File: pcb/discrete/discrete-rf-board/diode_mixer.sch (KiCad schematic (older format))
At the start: 30 parts, among them J30 UFL, J31 UFL, J32 UFL, J33 UFL, T5 HHM17147A1, T6 HHM17147A1, U22 BAT15-099R

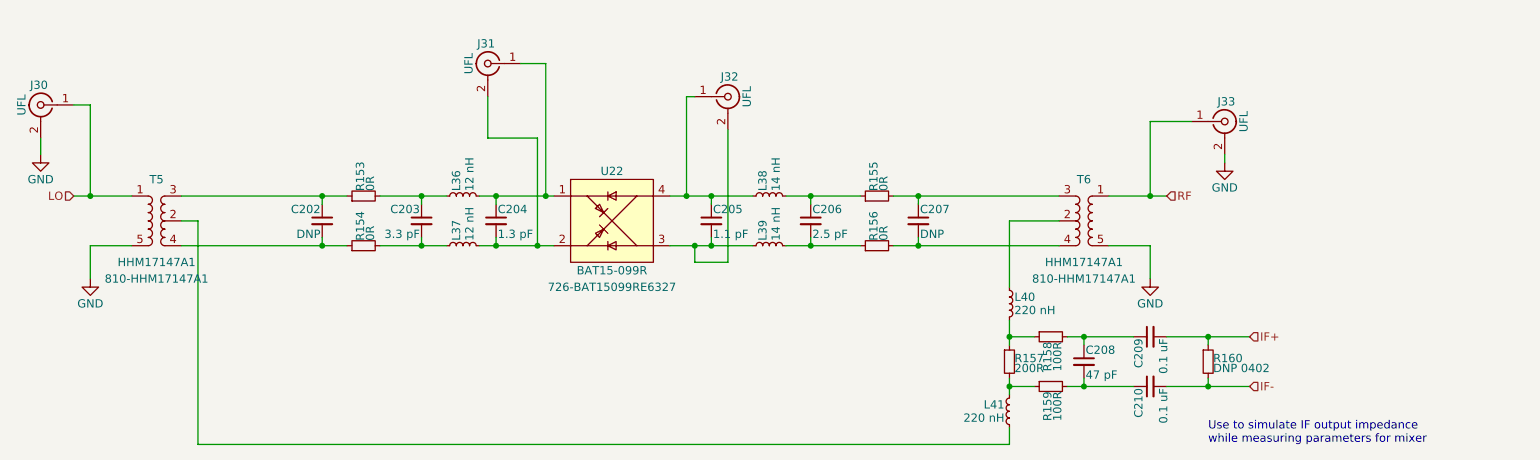
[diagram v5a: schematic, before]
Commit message: All component values set (TODO change transistor gain stages to match values from experimentation
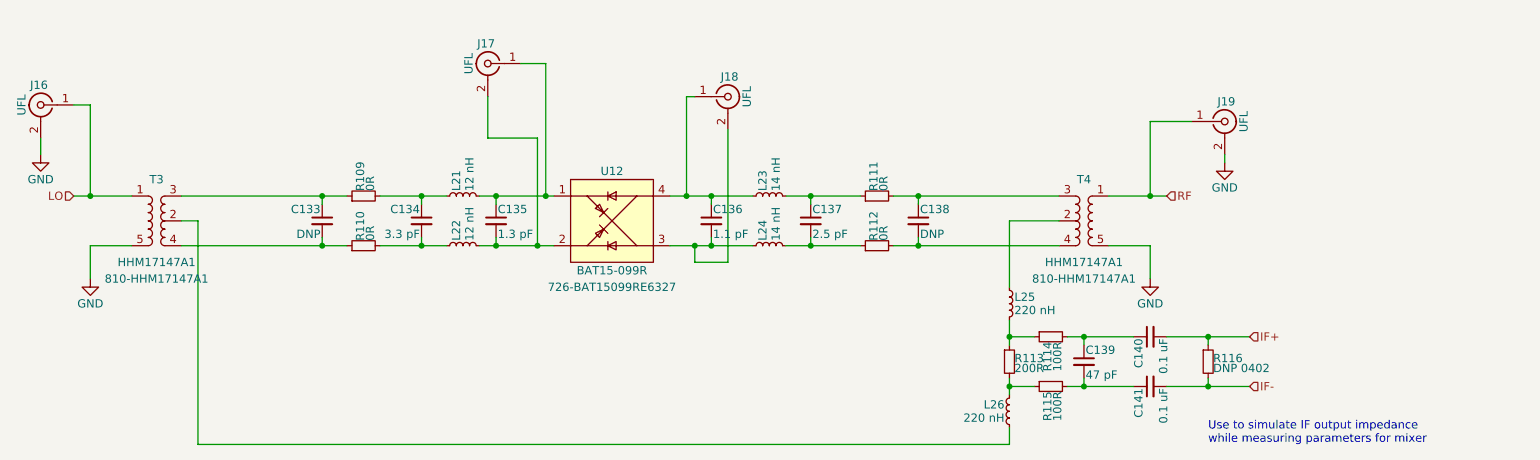
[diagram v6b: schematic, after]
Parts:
- T6: footprint (none) -> discrete_footprints:TDK_HHM17147A1
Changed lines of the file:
@@
 $Descr A4 11693 8268
 encoding utf-8
-Sheet 19 19
+Sheet 11 19
 Title ""
 Date ""
@@
 AR Path="/5CA6B0AA/5CC1CC09/5CC1E322" Ref="U22"  Part="1"
 AR Path="/5CA6B0AA/5CC4015A/5CC1E322" Ref="U12"  Part="1"
-F 0 "U22" H 5900 3900 50  0000 C CNN
+F 0 "U12" H 5900 3900 50  0000 C CNN
 F 1 "BAT15-099R" H 5900 3300 50  0000 C CNN
 F 2 "discrete_footprints:Infineon_SOT143" H 5900 3900 50  0001 C CNN
@@
 AR Path="/5CA6B0AA/5CC1CC09/5CC1F89D" Ref="C205"  Part="1"
 AR Path="/5CA6B0AA/5CC4015A/5CC1F89D" Ref="C136"  Part="1"
-F 0 "C205" H 6510 3670 50  0000 L CNN
+F 0 "C136" H 6510 3670 50  0000 L CNN
 F 1 "1.1 pF" H 6510 3520 50  0000 L CNN
 F 2 "" H 6500 3600 50  0001 C CNN
@@
 AR Path="/5CA6B0AA/5CC1CC09/5CC20238" Ref="C206"  Part="1"
 AR Path="/5CA6B0AA/5CC4015A/5CC20238" Ref="C137"  Part="1"
-F 0 "C206" H 7110 3670 50  0000 L CNN
+F 0 "C137" H 7110 3670 50  0000 L CNN
 F 1 "2.5 pF" H 7110 3520 50  0000 L CNN
 F 2 "" H 7100 3600 50  0001 C CNN
@@
 AR Path="/5CA6B0AA/5CC1CC09/5CC208EE" Ref="L39"  Part="1"
 AR Path="/5CA6B0AA/5CC4015A/5CC208EE" Ref="L24"  Part="1"
-F 0 "L39" H 6880 3790 50  0000 L CNN
+F 0 "L24" H 6880 3790 50  0000 L CNN
 F 1 "14 nH" H 6880 3710 50  0000 L CNN
 F 2 "" H 6850 3750 50  0001 C CNN
@@
 AR Path="/5CA6B0AA/5CC1CC09/5CC2101C" Ref="L38"  Part="1"
 AR Path="/5CA6B0AA/5CC4015A/5CC2101C" Ref="L23"  Part="1"
-F 0 "L38" H 6880 3490 50  0000 L CNN
+F 0 "L23" H 6880 3490 50  0000 L CNN
 F 1 "14 nH" H 6880 3410 50  0000 L CNN
 F 2 "" H 6850 3450 50  0001 C CNN
@@
 AR Path="/5CA6B0AA/5CC1CC09/5CC289D9" Ref="L40"  Part="1"
 AR Path="/5CA6B0AA/5CC4015A/5CC289D9" Ref="L25"  Part="1"
-F 0 "L40" H 8330 4140 50  0000 L CNN
+F 0 "L25" H 8330 4140 50  0000 L CNN
 F 1 "220 nH" H 8330 4060 50  0000 L CNN
 F 2 "" H 8300 4100 50  0001 C CNN
@@
 AR Path="/5CA6B0AA/5CC1CC09/5CC29B4E" Ref="R157"  Part="1"
 AR Path="/5CA6B0AA/5CC4015A/5CC29B4E" Ref="R113"  Part="1"
-F 0 "R157" H 8330 4470 50  0000 L CNN
+F 0 "R113" H 8330 4470 50  0000 L CNN
 F 1 "200R" H 8330 4410 50  0000 L CNN
 F 2 "" H 8300 4450 50  0001 C CNN
@@
 AR Path="/5CA6B0AA/5CC1CC09/5CC29F9D" Ref="R158"  Part="1"
 AR Path="/5CA6B0AA/5CC4015A/5CC29F9D" Ref="R114"  Part="1"
-F 0 "R158" H 8580 4320 50  0000 L CNN
+F 0 "R114" H 8580 4320 50  0000 L CNN
 F 1 "100R" H 8580 4260 50  0000 L CNN
 F 2 "" H 8550 4300 50  0001 C CNN
@@
 AR Path="/5CA6B0AA/5CC1CC09/5CC2B0AC" Ref="C208"  Part="1"
 AR Path="/5CA6B0AA/5CC4015A/5CC2B0AC" Ref="C139"  Part="1"
-F 0 "C208" H 8760 4520 50  0000 L CNN
+F 0 "C139" H 8760 4520 50  0000 L CNN
 F 1 "47 pF" H 8760 4370 50  0000 L CNN
 F 2 "" H 8750 4450 50  0001 C CNN
@@
 AR Path="/5CA6B0AA/5CC1CC09/5CC2FA5E" Ref="#PWR0257"  Part="1"
 AR Path="/5CA6B0AA/5CC4015A/5CC2FA5E" Ref="#PWR0169"  Part="1"
-F 0 "#PWR0257" H 2750 3700 50  0001 C CNN
+F 0 "#PWR0169" H 2750 3700 50  0001 C CNN
 F 1 "GND" H 2750 3800 50  0000 C CNN
 F 2 "" H 2750 3950 50  0001 C CNN
@@
 AR Path="/5CA6B0AA/5CC1CC09/5CC3011D" Ref="#PWR0258"  Part="1"
 AR Path="/5CA6B0AA/5CC4015A/5CC3011D" Ref="#PWR0170"  Part="1"
-F 0 "#PWR0258" H 9150 3700 50  0001 C CNN
+F 0 "#PWR0170" H 9150 3700 50  0001 C CNN
 F 1 "GND" H 9150 3800 50  0000 C CNN
 F 2 "" H 9150 3950 50  0001 C CNN
@@
 AR Path="/5CA6B0AA/5CC1CC09/5CC30B27" Ref="J30"  Part="1"
 AR Path="/5CA6B0AA/5CC4015A/5CC30B27" Ref="J16"  Part="1"
-F 0 "J30" H 2460 3020 50  0000 C CNN
+F 0 "J16" H 2460 3020 50  0000 C CNN
 F 1 "UFL" V 2565 2900 50  0000 C CNN
 F 2 "" H 2450 2900 50  0001 C CNN
@@
 AR Path="/5CA6B0AA/5CC1CC09/5CC31787" Ref="J33"  Part="1"
 AR Path="/5CA6B0AA/5CC4015A/5CC31787" Ref="J19"  Part="1"
-F 0 "J33" H 9610 3120 50  0000 C CNN
+F 0 "J19" H 9610 3120 50  0000 C CNN
 F 1 "UFL" V 9715 3000 50  0000 C CNN
 F 2 "" H 9600 3000 50  0001 C CNN
@@
 AR Path="/5CA6B0AA/5CC1CC09/5CC33186" Ref="#PWR0259"  Part="1"
 AR Path="/5CA6B0AA/5CC4015A/5CC33186" Ref="#PWR0171"  Part="1"
-F 0 "#PWR0259" H 9600 3000 50  0001 C CNN
+F 0 "#PWR0171" H 9600 3000 50  0001 C CNN
 F 1 "GND" H 9600 3100 50  0000 C CNN
 F 2 "" H 9600 3250 50  0001 C CNN
@@
 AR Path="/5CA6B0AA/5CC1CC09/5CC33A73" Ref="#PWR0256"  Part="1"
 AR Path="/5CA6B0AA/5CC4015A/5CC33A73" Ref="#PWR0168"  Part="1"
-F 0 "#PWR0256" H 2450 2950 50  0001 C CNN
+F 0 "#PWR0168" H 2450 2950 50  0001 C CNN
 F 1 "GND" H 2450 3050 50  0000 C CNN
 F 2 "" H 2450 3200 50  0001 C CNN
@@
 AR Path="/5CA6B0AA/5CC1CC09/5CC5AE0B" Ref="L41"  Part="1"
 AR Path="/5CA6B0AA/5CC4015A/5CC5AE0B" Ref="L26"  Part="1"
-F 0 "L41" H 8330 4790 50  0000 L CNN
+F 0 "L26" H 8330 4790 50  0000 L CNN
 F 1 "220 nH" H 8330 4710 50  0000 L CNN
 F 2 "" H 8300 4750 50  0001 C CNN
@@
 AR Path="/5CA6B0AA/5CC1CC09/5CC5DD55" Ref="R159"  Part="1"
 AR Path="/5CA6B0AA/5CC4015A/5CC5DD55" Ref="R115"  Part="1"
-F 0 "R159" H 8580 4620 50  0000 L CNN
+F 0 "R115" H 8580 4620 50  0000 L CNN
 F 1 "100R" H 8580 4560 50  0000 L CNN
 F 2 "" H 8550 4600 50  0001 C CNN
@@
 AR Path="/5CA6B0AA/5CC1CC09/5CC22010" Ref="L37"  Part="1"
 AR Path="/5CA6B0AA/5CC4015A/5CC22010" Ref="L22"  Part="1"
-F 0 "L37" H 5030 3790 50  0000 L CNN
+F 0 "L22" H 5030 3790 50  0000 L CNN
 F 1 "12 nH" H 5030 3710 50  0000 L CNN
 F 2 "" H 5000 3750 50  0001 C CNN
@@
 AR Path="/5CA6B0AA/5CC1CC09/5CC1F7BA" Ref="C203"  Part="1"
 AR Path="/5CA6B0AA/5CC4015A/5CC1F7BA" Ref="C134"  Part="1"
-F 0 "C203" H 4760 3670 50  0000 L CNN
+F 0 "C134" H 4760 3670 50  0000 L CNN
 F 1 "3.3 pF" H 4760 3520 50  0000 L CNN
 F 2 "" H 4750 3600 50  0001 C CNN
@@
 AR Path="/5CA6B0AA/5CC1CC09/5CC1E94D" Ref="C204"  Part="1"
 AR Path="/5CA6B0AA/5CC4015A/5CC1E94D" Ref="C135"  Part="1"
-F 0 "C204" H 5210 3670 50  0000 L CNN
+F 0 "C135" H 5210 3670 50  0000 L CNN
 F 1 "1.3 pF" H 5210 3520 50  0000 L CNN
 F 2 "" H 5200 3600 50  0001 C CNN
@@
 AR Path="/5CA6B0AA/5CC1CC09/5CC22016" Ref="L36"  Part="1"
 AR Path="/5CA6B0AA/5CC4015A/5CC22016" Ref="L21"  Part="1"
-F 0 "L36" H 5030 3490 50  0000 L CNN
+F 0 "L21" H 5030 3490 50  0000 L CNN
 F 1 "12 nH" H 5030 3410 50  0000 L CNN
 F 2 "" H 5000 3450 50  0001 C CNN
@@
 AR Path="/5CA6B0AA/5CC1CC09/5D51EF09" Ref="C202"  Part="1"
 AR Path="/5CA6B0AA/5CC4015A/5D51EF09" Ref="C133"  Part="1"
-F 0 "C202" H 4160 3670 50  0000 L CNN
+F 0 "C133" H 4160 3670 50  0000 L CNN
 F 1 "DNP" H 4160 3520 50  0000 L CNN
 F 2 "" H 4150 3600 50  0001 C CNN
@@
 AR Path="/5CA6B0AA/5CC1CC09/5D51FC82" Ref="R153"  Part="1"
 AR Path="/5CA6B0AA/5CC4015A/5D51FC82" Ref="R109"  Part="1"
-F 0 "R153" H 4430 3470 50  0000 L CNN
+F 0 "R109" H 4430 3470 50  0000 L CNN
 F 1 "0R" H 4430 3410 50  0000 L CNN
 F 2 "" H 4400 3450 50  0001 C CNN
@@
 AR Path="/5CA6B0AA/5CC1CC09/5D5221DB" Ref="R154"  Part="1"
 AR Path="/5CA6B0AA/5CC4015A/5D5221DB" Ref="R110"  Part="1"
-F 0 "R154" H 4430 3770 50  0000 L CNN
+F 0 "R110" H 4430 3770 50  0000 L CNN
 F 1 "0R" H 4430 3710 50  0000 L CNN
 F 2 "" H 4400 3750 50  0001 C CNN
@@
 AR Path="/5CA6B0AA/5CC1CC09/5D52D7BD" Ref="C207"  Part="1"
 AR Path="/5CA6B0AA/5CC4015A/5D52D7BD" Ref="C138"  Part="1"
-F 0 "C207" H 7760 3670 50  0000 L CNN
+F 0 "C138" H 7760 3670 50  0000 L CNN
 F 1 "DNP" H 7760 3520 50  0000 L CNN
 F 2 "" H 7750 3600 50  0001 C CNN
@@
 AR Path="/5CA6B0AA/5CC1CC09/5D52D7C3" Ref="R155"  Part="1"
 AR Path="/5CA6B0AA/5CC4015A/5D52D7C3" Ref="R111"  Part="1"
-F 0 "R155" H 7530 3470 50  0000 L CNN
+F 0 "R111" H 7530 3470 50  0000 L CNN
 F 1 "0R" H 7530 3410 50  0000 L CNN
 F 2 "" H 7500 3450 50  0001 C CNN
@@
 AR Path="/5CA6B0AA/5CC1CC09/5D52D7C9" Ref="R156"  Part="1"
 AR Path="/5CA6B0AA/5CC4015A/5D52D7C9" Ref="R112"  Part="1"
-F 0 "R156" H 7530 3770 50  0000 L CNN
+F 0 "R112" H 7530 3770 50  0000 L CNN
 F 1 "0R" H 7530 3710 50  0000 L CNN
 F 2 "" H 7500 3750 50  0001 C CNN
@@
 AR Path="/5CA6B0AA/5CC1CC09/5D1B92FB" Ref="T5"  Part="1"
 AR Path="/5CA6B0AA/5CC4015A/5D1B92FB" Ref="T3"  Part="1"
-F 0 "T5" H 3150 3850 50  0000 C CNN
+F 0 "T3" H 3150 3850 50  0000 C CNN
 F 1 "HHM17147A1" H 3150 3350 50  0000 C CNN
 F 2 "" H 3150 3850 50  0001 C CNN
@@
 AR Path="/5CA6B0AA/5CC1CC09/5D1C03F7" Ref="T6"  Part="1"
 AR Path="/5CA6B0AA/5CC4015A/5D1C03F7" Ref="T4"  Part="1"
-F 0 "T6" H 8750 3850 50  0000 C CNN
+F 0 "T4" H 8750 3850 50  0000 C CNN
 F 1 "HHM17147A1" H 8750 3350 50  0000 C CNN
-F 2 "" H 8750 3850 50  0001 C CNN
+F 2 "discrete_footprints:TDK_HHM17147A1" H 8750 3850 50  0001 C CNN
 F 3 "" H 8750 3850 50  0001 C CNN
 F 4 "810-HHM17147A1" H 8750 3250 50  0000 C CNN "Mouser"
@@
 AR Path="/5CA6B0AA/5CC1CC09/5D264607" Ref="J31"  Part="1"
 AR Path="/5CA6B0AA/5CC4015A/5D264607" Ref="J17"  Part="1"
-F 0 "J31" H 5160 2770 50  0000 C CNN
+F 0 "J17" H 5160 2770 50  0000 C CNN
 F 1 "UFL" V 5265 2650 50  0000 C CNN
 F 2 "" H 5150 2650 50  0001 C CNN
@@
 AR Path="/5CA6B0AA/5CC1CC09/5D264D0A" Ref="J32"  Part="1"
 AR Path="/5CA6B0AA/5CC4015A/5D264D0A" Ref="J18"  Part="1"
-F 0 "J32" H 6610 2970 50  0000 C CNN
+F 0 "J18" H 6610 2970 50  0000 C CNN
 F 1 "UFL" V 6715 2850 50  0000 C CNN
 F 2 "" H 6600 2850 50  0001 C CNN
@@
 AR Path="/5CA6B0AA/5CC1CC09/5D979A64" Ref="R160"  Part="1"
 AR Path="/5CA6B0AA/5CC4015A/5D979A64" Ref="R116"  Part="1"
-F 0 "R160" H 9530 4470 50  0000 L CNN
+F 0 "R116" H 9530 4470 50  0000 L CNN
 F 1 "DNP 0402" H 9530 4410 50  0000 L CNN
 F 2 "" H 9500 4450 50  0001 C CNN
@@
 AR Path="/5CA6B0AA/5CC4015A/5DDA2DE4" Ref="C140"  Part="1"
 AR Path="/5CA6B0AA/5CC1CC09/5DDA2DE4" Ref="C209"  Part="1"
-F 0 "C209" H 9160 4370 50  0000 L CNN
+F 0 "C140" H 9160 4370 50  0000 L CNN
 F 1 "0.1 uF" H 9160 4220 50  0000 L CNN
 F 2 "" H 9150 4300 50  0001 C CNN
@@
 AR Path="/5CA6B0AA/5CC4015A/5DDA597D" Ref="C141"  Part="1"
 AR Path="/5CA6B0AA/5CC1CC09/5DDA597D" Ref="C210"  Part="1"
-F 0 "C210" H 9160 4670 50  0000 L CNN
+F 0 "C141" H 9160 4670 50  0000 L CNN
 F 1 "0.1 uF" H 9160 4520 50  0000 L CNN
 F 2 "" H 9150 4600 50  0001 C CNN

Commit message: Autofill; lots left to do
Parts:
- J30, J31, J32, J33: footprint (none) -> discrete_footprints:2337019-1; Mouser (none) -> 571-2337019-1
- T5: footprint (none) -> discrete_footprints:TDK_HHM17147A1
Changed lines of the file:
@@
 AR Path="/5CA6B0AA/5CC1CC09/5CC2FA5E" Ref="#PWR0257"  Part="1"
 AR Path="/5CA6B0AA/5CC4015A/5CC2FA5E" Ref="#PWR0169"  Part="1"
-F 0 "#PWR0169" H 2750 3700 50  0001 C CNN
+F 0 "#PWR0257" H 2750 3700 50  0001 C CNN
 F 1 "GND" H 2750 3800 50  0000 C CNN
 F 2 "" H 2750 3950 50  0001 C CNN
@@
 AR Path="/5CA6B0AA/5CC1CC09/5CC3011D" Ref="#PWR0258"  Part="1"
 AR Path="/5CA6B0AA/5CC4015A/5CC3011D" Ref="#PWR0170"  Part="1"
-F 0 "#PWR0170" H 9150 3700 50  0001 C CNN
+F 0 "#PWR0258" H 9150 3700 50  0001 C CNN
 F 1 "GND" H 9150 3800 50  0000 C CNN
 F 2 "" H 9150 3950 50  0001 C CNN
@@
 F 0 "J16" H 2460 3020 50  0000 C CNN
 F 1 "UFL" V 2565 2900 50  0000 C CNN
-F 2 "" H 2450 2900 50  0001 C CNN
+F 2 "discrete_footprints:2337019-1" H 2450 2900 50  0001 C CNN
 F 3 " ~" H 2450 2900 50  0001 C CNN
+F 4 " 571-2337019-1" H 2450 2900 50  0001 C CNN "Mouser"
 	1    2450 2900
 	-1   0    0    -1
@@
 F 0 "J19" H 9610 3120 50  0000 C CNN
 F 1 "UFL" V 9715 3000 50  0000 C CNN
-F 2 "" H 9600 3000 50  0001 C CNN
+F 2 "discrete_footprints:2337019-1" H 9600 3000 50  0001 C CNN
 F 3 " ~" H 9600 3000 50  0001 C CNN
+F 4 " 571-2337019-1" H 9600 3000 50  0001 C CNN "Mouser"
 	1    9600 3000
 	1    0    0    -1
@@
 AR Path="/5CA6B0AA/5CC1CC09/5CC33186" Ref="#PWR0259"  Part="1"
 AR Path="/5CA6B0AA/5CC4015A/5CC33186" Ref="#PWR0171"  Part="1"
-F 0 "#PWR0171" H 9600 3000 50  0001 C CNN
+F 0 "#PWR0259" H 9600 3000 50  0001 C CNN
 F 1 "GND" H 9600 3100 50  0000 C CNN
 F 2 "" H 9600 3250 50  0001 C CNN
@@
 AR Path="/5CA6B0AA/5CC1CC09/5CC33A73" Ref="#PWR0256"  Part="1"
 AR Path="/5CA6B0AA/5CC4015A/5CC33A73" Ref="#PWR0168"  Part="1"
-F 0 "#PWR0168" H 2450 2950 50  0001 C CNN
+F 0 "#PWR0256" H 2450 2950 50  0001 C CNN
 F 1 "GND" H 2450 3050 50  0000 C CNN
 F 2 "" H 2450 3200 50  0001 C CNN
@@
 F 0 "T3" H 3150 3850 50  0000 C CNN
 F 1 "HHM17147A1" H 3150 3350 50  0000 C CNN
-F 2 "" H 3150 3850 50  0001 C CNN
+F 2 "discrete_footprints:TDK_HHM17147A1" H 3150 3850 50  0001 C CNN
 F 3 "" H 3150 3850 50  0001 C CNN
 F 4 "810-HHM17147A1" H 3150 3250 50  0000 C CNN "Mouser"
@@
 F 0 "J17" H 5160 2770 50  0000 C CNN
 F 1 "UFL" V 5265 2650 50  0000 C CNN
-F 2 "" H 5150 2650 50  0001 C CNN
+F 2 "discrete_footprints:2337019-1" H 5150 2650 50  0001 C CNN
 F 3 " ~" H 5150 2650 50  0001 C CNN
+F 4 " 571-2337019-1" H 5150 2650 50  0001 C CNN "Mouser"
 	1    5150 2650
 	-1   0    0    -1
@@
 F 0 "J18" H 6610 2970 50  0000 C CNN
 F 1 "UFL" V 6715 2850 50  0000 C CNN
-F 2 "" H 6600 2850 50  0001 C CNN
+F 2 "discrete_footprints:2337019-1" H 6600 2850 50  0001 C CNN
 F 3 " ~" H 6600 2850 50  0001 C CNN
+F 4 " 571-2337019-1" H 6600 2850 50  0001 C CNN "Mouser"
 	1    6600 2850
 	1    0    0    -1

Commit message: Footprint some stuff
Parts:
- C205: footprint (none) -> Capacitor_SMD:C_0402_1005Metric; Mouser (none) -> 791-RF15N1R1B500CT
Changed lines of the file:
@@
 F 0 "C136" H 6510 3670 50  0000 L CNN
 F 1 "1.1 pF" H 6510 3520 50  0000 L CNN
-F 2 "" H 6500 3600 50  0001 C CNN
+F 2 "Capacitor_SMD:C_0402_1005Metric" H 6500 3600 50  0001 C CNN
 F 3 "~" H 6500 3600 50  0001 C CNN
+F 4 "791-RF15N1R1B500CT" H 6500 3600 50  0001 C CNN "Mouser"
 	1    6500 3600
 	1    0    0    -1
@@
 AR Path="/5CA6B0AA/5CC1CC09/5CC2FA5E" Ref="#PWR0257"  Part="1"
 AR Path="/5CA6B0AA/5CC4015A/5CC2FA5E" Ref="#PWR0169"  Part="1"
-F 0 "#PWR0257" H 2750 3700 50  0001 C CNN
+F 0 "#PWR0169" H 2750 3700 50  0001 C CNN
 F 1 "GND" H 2750 3800 50  0000 C CNN
 F 2 "" H 2750 3950 50  0001 C CNN
@@
 AR Path="/5CA6B0AA/5CC1CC09/5CC3011D" Ref="#PWR0258"  Part="1"
 AR Path="/5CA6B0AA/5CC4015A/5CC3011D" Ref="#PWR0170"  Part="1"
-F 0 "#PWR0258" H 9150 3700 50  0001 C CNN
+F 0 "#PWR0170" H 9150 3700 50  0001 C CNN
 F 1 "GND" H 9150 3800 50  0000 C CNN
 F 2 "" H 9150 3950 50  0001 C CNN
@@
 AR Path="/5CA6B0AA/5CC1CC09/5CC33186" Ref="#PWR0259"  Part="1"
 AR Path="/5CA6B0AA/5CC4015A/5CC33186" Ref="#PWR0171"  Part="1"
-F 0 "#PWR0259" H 9600 3000 50  0001 C CNN
+F 0 "#PWR0171" H 9600 3000 50  0001 C CNN
 F 1 "GND" H 9600 3100 50  0000 C CNN
 F 2 "" H 9600 3250 50  0001 C CNN
@@
 AR Path="/5CA6B0AA/5CC1CC09/5CC33A73" Ref="#PWR0256"  Part="1"
 AR Path="/5CA6B0AA/5CC4015A/5CC33A73" Ref="#PWR0168"  Part="1"
-F 0 "#PWR0256" H 2450 2950 50  0001 C CNN
+F 0 "#PWR0168" H 2450 2950 50  0001 C CNN
 F 1 "GND" H 2450 3050 50  0000 C CNN
 F 2 "" H 2450 3200 50  0001 C CNN
